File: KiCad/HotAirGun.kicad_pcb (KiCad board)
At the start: 2 copper layers, 49.8 x 17.6 mm, 22 parts, among them J4 Arduino_Nano_Header, Q2 SI2308, SW1 Rotary_Encoder, U1 MAX31855K

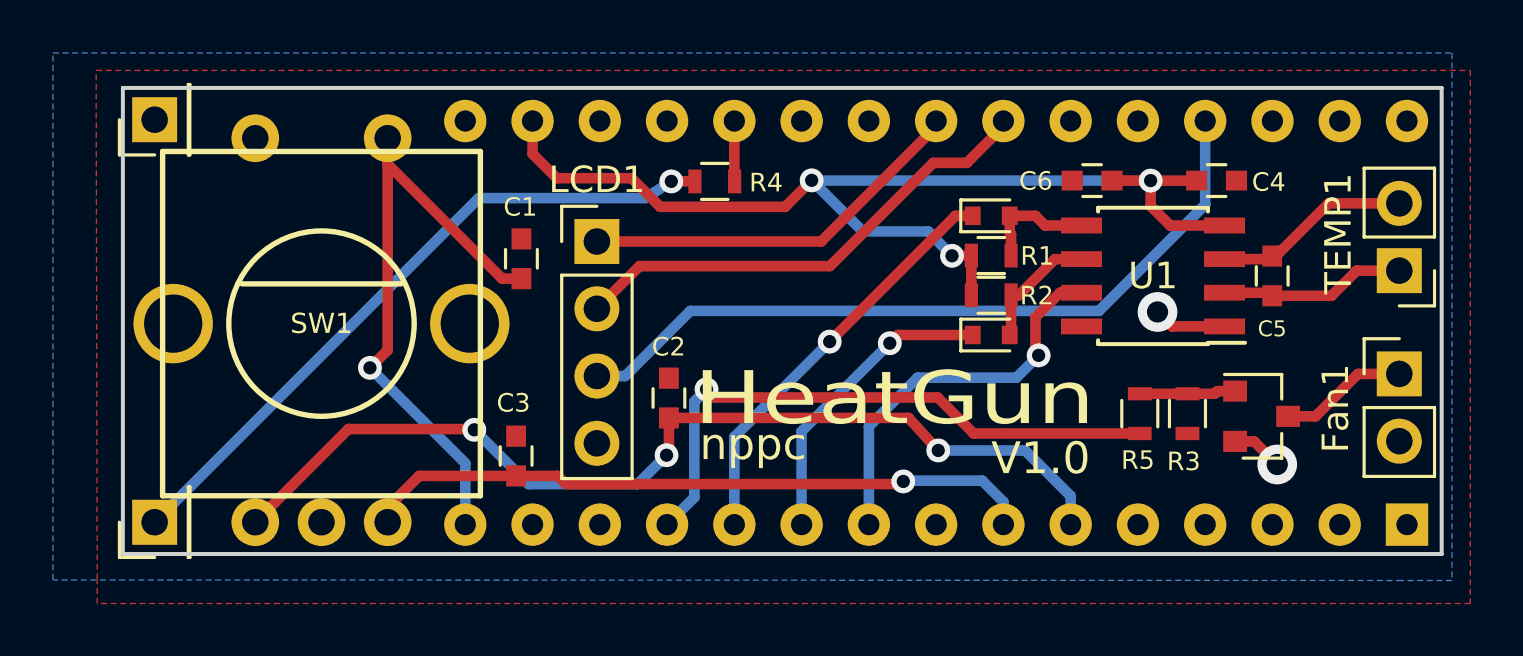
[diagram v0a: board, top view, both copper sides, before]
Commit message: SOD123 diodes
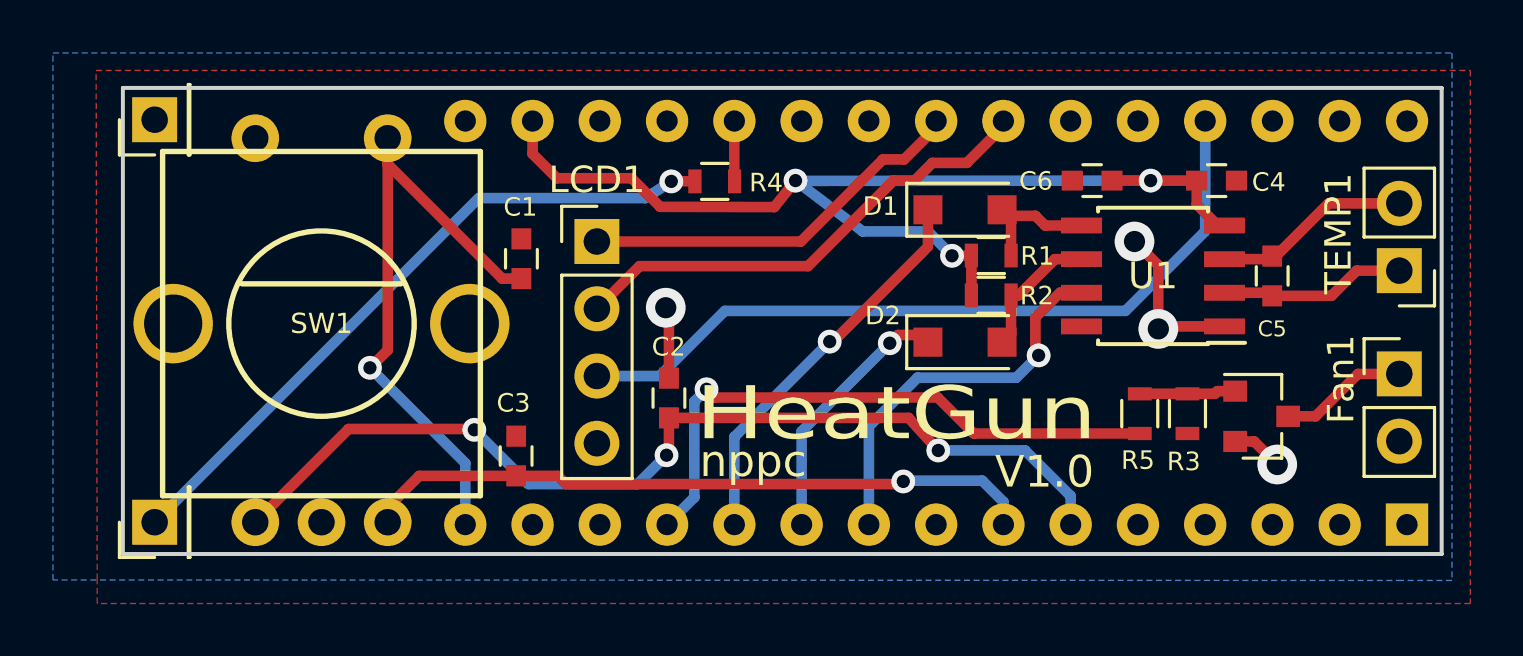
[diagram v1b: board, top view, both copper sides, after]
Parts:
- D1, D2: footprint Diodes_SMD:D_SOD-523 -> Diodes_SMD:D_SOD-123F
- moved D2 1.03 mm to (155.1, 128.1)
- moved D1 1.02 mm to (155.1, 123.1)
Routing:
- net GND: track 4.71 -> 11.0 mm, vias 2 -> 4
- net /T_CS: track 11.5 -> 9.87 mm
- net +3V3: track 41.8 -> 40.6 mm
- net /T_SCK: track 15.8 -> 14.9 mm
- net VCC: track 28.8 -> 29.4 mm
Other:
- rule pad_to_mask_clearance: 0.2 -> 0.1
- board text added: "+24V"
- board text added: "+3.3V"
